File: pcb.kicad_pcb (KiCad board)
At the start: 2 copper layers, 88 x 53 mm, 40 parts, among them J1 TYPE-C-31-M-12, Q1 FDN339AN, SW1 SW_SPST, U1 WeMos_D1_mini, U2 TSOP38236, U3 MCP73831-2-OT, U4 BQ27441DRZR-G1A, U5 TLV75733PDBV

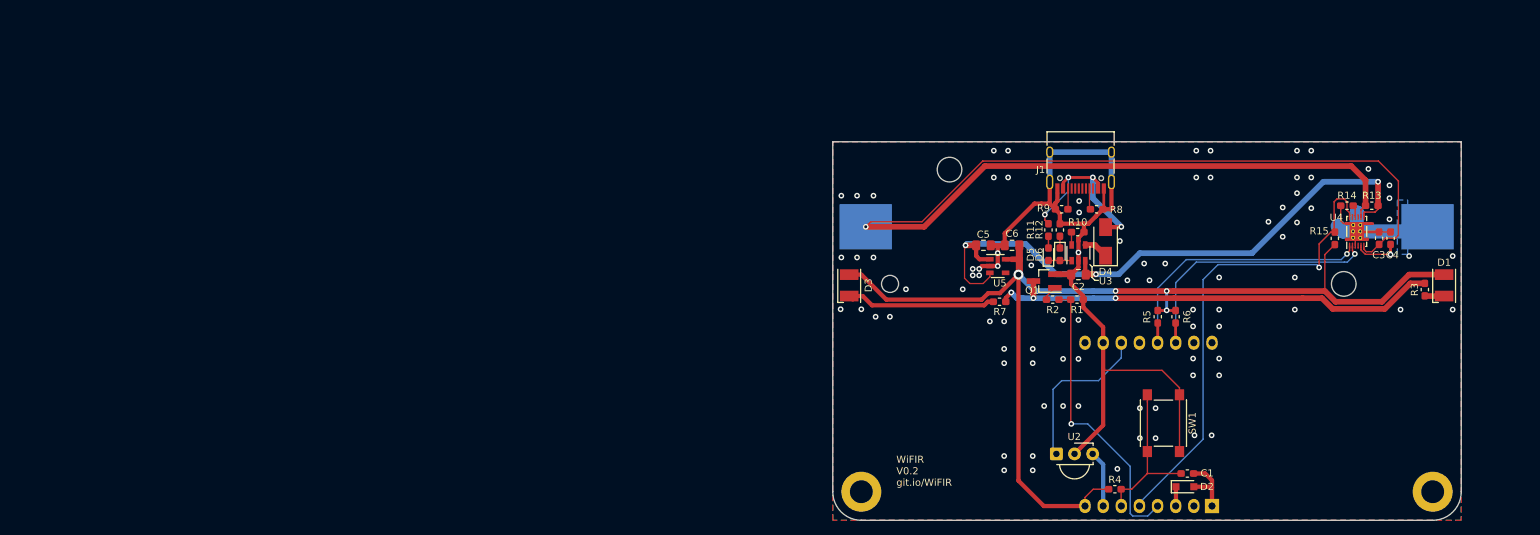
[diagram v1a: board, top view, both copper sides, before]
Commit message: Redesigned to small-stick formfactor
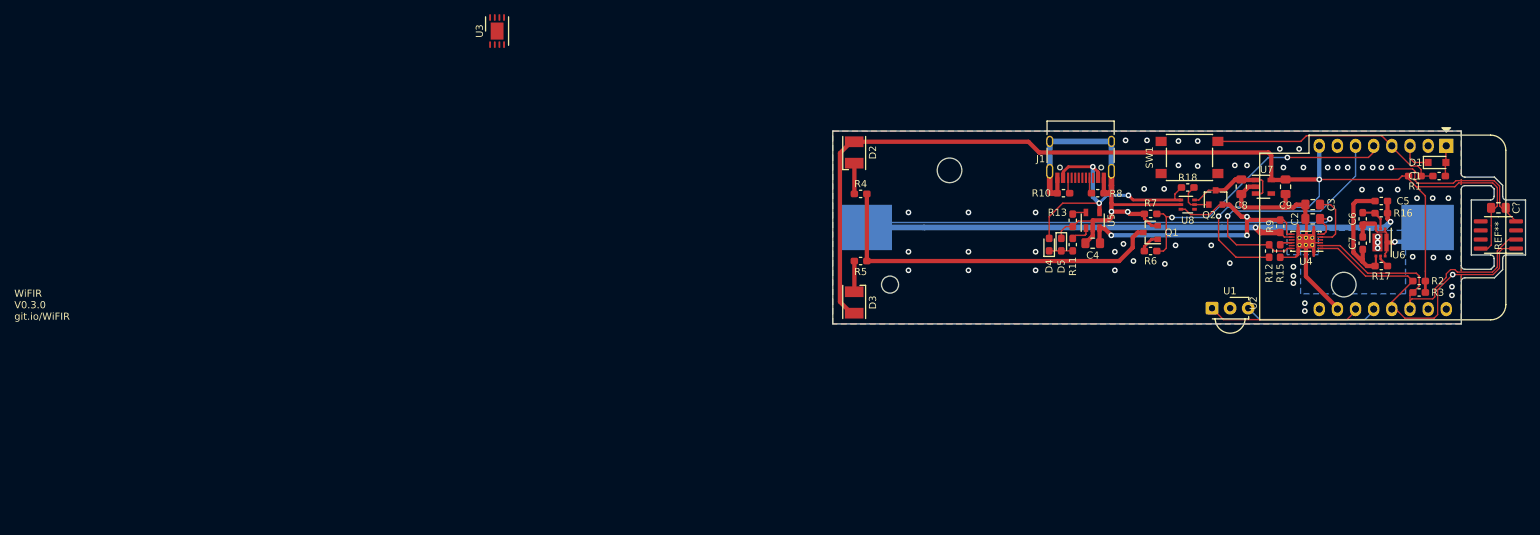
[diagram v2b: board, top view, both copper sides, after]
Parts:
- removed the C3 at (250.5, 77.5)
- removed D6: charged, LED_SMD:LED_0603_1608Metric_Pad1.05x0.95mm_HandSolder
- removed G*** (x2): LOGO, Personal_graphics:kiwi12.5mm
- removed the R15 at (244.3, 77.5)
- removed the REF** at (178.0, 113.0)
- removed the REF** at (258.0, 113.0)
- added C4: 4.7uF, Capacitor_SMD:C_0805_2012Metric_Pad1.15x1.40mm_HandSolder, F.Cu at (210.4, 78.2)
- added C7: 100nF, Capacitor_SMD:C_0603_1608Metric_Pad1.05x0.95mm_HandSolder, F.Cu at (248.2, 78.2)
- added C8: 4.7uF, Capacitor_SMD:C_0805_2012Metric_Pad1.15x1.40mm_HandSolder, F.Cu at (231.2, 70.3)
- added C9: 4.7uF, Capacitor_SMD:C_0805_2012Metric_Pad1.15x1.40mm_HandSolder, F.Cu at (237.4, 70.3)
- added C?: 10nF, Capacitor_SMD:C_0805_2012Metric_Pad1.15x1.40mm_HandSolder, F.Cu at (267.2, 73.2)
- added Q2: SI2333, Package_TO_SOT_SMD:SOT-23, F.Cu at (227.6, 71.8)
- added R16: 680R, Resistor_SMD:R_0603_1608Metric_Pad1.05x0.95mm_HandSolder, F.Cu at (250.8, 74.0)
- added R17: 1K, Resistor_SMD:R_0603_1608Metric_Pad1.05x0.95mm_HandSolder, F.Cu at (250.8, 81.4)
- added R18: 10k, Resistor_SMD:R_0603_1608Metric_Pad1.05x0.95mm_HandSolder, F.Cu at (223.7, 70.4)
- added REF**: SOIC-8_3.9x4.9mm_P1.27mm, Package_SO:SOIC-8_3.9x4.9mm_P1.27mm, F.Cu at (267.2, 77.0)
- added U6: LC05111C02MTTTG, Package_DFN_QFN:OnSemi_WDFN-6-2EP_2.6x4.0mm_P0.65mm, F.Cu at (250.7, 78.1)
- added U7: TLV75733PDBV, Package_TO_SOT_SMD:SOT-23-5, F.Cu at (234.3, 70.3)
- added U8: LM66100, Package_TO_SOT_SMD:SOT-363_SC-70-6, F.Cu at (223.7, 72.8)
- BT1: value protected 18650 -> Li-ion 3.7v
- C2: value 4.7uF -> 10nF
- C3: renamed from C4; footprint Capacitor_SMD:C_0603_1608Metric_Pad1.05x0.95mm_HandSolder -> Capacitor_SMD:C_0805_2012Metric_Pad1.15x1.40mm_HandSolder
- C5, C6: value 4.7uF -> 100nF; footprint Capacitor_SMD:C_0805_2012Metric_Pad1.15x1.40mm_HandSolder -> Capacitor_SMD:C_0603_1608Metric_Pad1.05x0.95mm_HandSolder
- D1: value VSML3710-GS18 -> BAT54WS; footprint LED_SMD:LED_PLCC-2 -> Diode_SMD:D_SOD-323_HandSoldering
- D2: value BAT54WS -> VSML3710-GS18; footprint Diode_SMD:D_SOD-323_HandSoldering -> LED_SMD:LED_PLCC-2
- D4: value MBRA140 -> charging; footprint Diode_SMD:D_SMA -> LED_SMD:LED_0603_1608Metric_Pad1.05x0.95mm_HandSolder
- D5: value charging -> charged
- Q1: footprint Package_TO_SOT_SMD:SOT-23_Handsoldering -> Package_TO_SOT_SMD:SOT-23
- R1: value 4k7 -> 10k
- R10: value 10k -> 5k1
- R12: value 470R -> 10k
- R13: value 10mR -> 2k2
- R2: value 1k -> 4k7
- R3, R7: value 6R8 -> 4k7
- R4: value 10k -> 6R8
- R5: value 4k7 -> 6R8
- R6: value 4k7 -> 1k
- R9: value 5k1 -> 10mR
- U1: value WeMos_D1_mini -> TSOP38236; footprint Module:WEMOS_D1_mini_light -> OptoDevice:Vishay_MINICAST-3Pin; moved to F.Cu
- U2: value TSOP38236 -> WeMos_D1_mini; footprint OptoDevice:Vishay_MINICAST-3Pin -> Module:WEMOS_D1_mini_light
- U3: value MCP73831-2-OT -> LC709203FQH-01TWG; footprint Package_TO_SOT_SMD:SOT-23-5 -> Package_DFN_QFN:WDFN-8-1EP_4x3mm_P0.65mm_EP2.4x1.8mm
- U5: value TLV75733PDBV -> MCP73831-2-OT
- moved U3 87.1 mm to (127.0, 48.5)
- moved U2 69.6 mm to (259.9, 64.6), turned to 270 degrees
- moved D2 65.8 mm to (177.0, 65.5), turned to 90 degrees
- moved C5 56.0 mm to (250.8, 72.3)
- moved C1 54.6 mm to (258.9, 68.8)
- moved R4 54.6 mm to (177.9, 71.3), turned to 0 degrees
- moved R2 51.4 mm to (256.1, 83.5), turned to 0 degrees
- moved R1 50.4 mm to (255.5, 68.8)
- moved C6 49.2 mm to (248.2, 74.8), turned to 90 degrees
- moved R5 42.3 mm to (177.9, 80.7), turned to 0 degrees
- moved R13 41.9 mm to (207.6, 75.0), turned to 90 degrees
- moved SW1 37.4 mm to (223.9, 66.2), turned to 180 degrees
- moved C2 33.7 mm to (241.2, 74.8)
- moved R9 30.7 mm to (236.7, 75.8), turned to 90 degrees
- moved R12 29.4 mm to (235.1, 79.3), turned to 270 degrees
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- renumbered R14 to R15
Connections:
- BT1 pad 2: GND -> -BATT
- C2 pad 2: VCCQ -> +BATT
- C5 pad 1: VCCQ -> GND
- C5 pad 2: GND -> +BATT
- C6 pad 1: GND -> -BATT
- C6 pad 2: +3V3 -> Net-(C6-Pad2)
- D1 pad 1: Net-(D1-Pad1) -> device_wake
- D1 pad 2: +3V3 -> ~RST
- D2 pad 1: device_wake -> Net-(D2-Pad1)
- D2 pad 2: ~RST -> +3V3
- D5 pad 1: Net-(D5-Pad1) -> GND
- D5 pad 2: Net-(D5-Pad2) -> Net-(D4-Pad1)
- R1 pad 1: GND -> factory_rst
- R1 pad 2: IR_BLAST -> +3V3
- R10 pad 2: Net-(R10-Pad2) -> Net-(J1-PadB5)
- R11 pad 1: VBUS -> Net-(D4-Pad1)
- R11 pad 2: Net-(D5-Pad2) -> Net-(R11-Pad2)
- R12 pad 1: Net-(D6-Pad1) -> ~LOW_BAT
- R12 pad 2: GND -> +3V3
- R13 pad 1: +BATT -> GND
- R13 pad 2: VCCQ -> Net-(R13-Pad2)
- R2 pad 1: IR_BLAST -> /MCU + I/O/SDA
- R2 pad 2: Net-(Q1-Pad1) -> +3V3
- R3 pad 1: Net-(D1-Pad1) -> /MCU + I/O/SCL
- R3 pad 2: Net-(Q1-Pad3) -> +3V3
- R4 pad 1: factory_rst -> Net-(D2-Pad1)
- R4 pad 2: +3V3 -> Net-(Q1-Pad3)
- R5 pad 1: SDA -> Net-(D3-Pad1)
- R5 pad 2: +3V3 -> Net-(Q1-Pad3)
- R6 pad 1: SCL -> IR_BLAST
- R6 pad 2: +3V3 -> Net-(Q1-Pad1)
- R7 pad 1: Net-(D3-Pad1) -> GND
- R7 pad 2: Net-(Q1-Pad3) -> IR_BLAST
- R9 pad 1: GND -> +BATT
- R9 pad 2: Net-(J1-PadB5) -> Net-(C4-Pad2)
- U1 pad 1: ~RST -> IR_SIGNAL
- U1 pad 2: Net-(U1-Pad2) -> GND
- U1 pad 3: device_wake -> IR_RECV_VCC
- U2 pad 1: IR_SIGNAL -> ~RST
- U2 pad 2: GND -> Net-(U2-Pad2)
- U2 pad 3: IR_RECV_VCC -> device_wake
- U3 pad 1: Net-(D5-Pad1) -> Net-(U3-Pad1)
- U3 pad 2: GND -> Net-(U3-Pad2)
- U3 pad 3: VCCQ -> Net-(U3-Pad3)
- U3 pad 4: Net-(D4-Pad1) -> Net-(U3-Pad4)
- U3 pad 5: Net-(R10-Pad2) -> Net-(U3-Pad5)
- U4 pad 1: SDA -> /MCU + I/O/SDA
- U4 pad 2: SCL -> /MCU + I/O/SCL
- U4 pad 7: VCCQ -> Net-(C4-Pad2)
- U5 pad 1: VCCQ -> Net-(R11-Pad2)
- U5 pad 3: VCCQ -> Net-(C4-Pad2)
- U5 pad 4: Net-(U5-Pad4) -> VBUS
- U5 pad 5: +3V3 -> Net-(R13-Pad2)
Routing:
- net VCCQ: track 89.6 -> 0.00 mm, vias 3 -> 0
- net /MCU + I/O/SDA: track 0.00 -> 45.5 mm, vias 0 -> 1
- net Net-(C4-Pad2): track 0.00 -> 44.8 mm, vias 0 -> 3
- net /MCU + I/O/SCL: track 0.00 -> 42.9 mm
- net SDA: track 40.3 -> 0.00 mm, vias 1 -> 0
- net SCL: track 39.4 -> 0.00 mm, vias 1 -> 0
- net ~LOW_BAT: track 67.6 -> 37.3 mm
- net +3V3: track 152.3 -> 181.7 mm, vias 4 -> 2
- net +BATT: track 173.7 -> 154.2 mm, vias 1 -> 3
- net Net-(D3-Pad1): track 21.6 -> 4.31 mm
- net -BATT: track 0.00 -> 17.1 mm, vias 0 -> 1
- net VBUS: track 26.2 -> 40.4 mm, vias 4 -> 3
- net Net-(Q1-Pad3): track 64.4 -> 50.6 mm, vias 3 -> 0
- net Net-(C8-Pad1): track 0.00 -> 13.5 mm
- net IR_RECV_VCC: track 7.91 -> 19.0 mm
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- added copper zone on B.Cu, net Net-(U6-Pad7)
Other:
- board size 88 x 53 mm -> 97 x 27 mm
- board text added: "WiFIR V0.3.0 git.io/WiFIR"
- board text removed: "JLCJLCJLCJLC"
- board text removed: "WiFIR V0.2 git.io/WiFIR"

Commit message: Added alternative fuel gauge to PCB
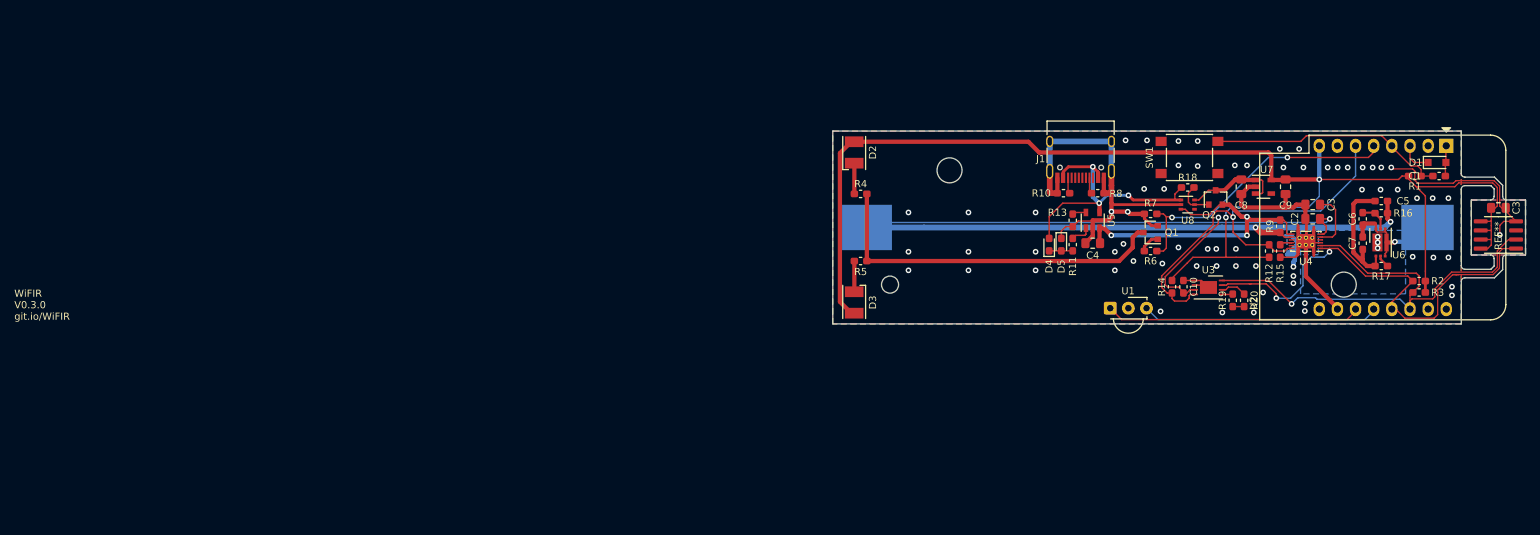
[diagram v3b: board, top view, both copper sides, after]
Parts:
- added C10: 1uF, Capacitor_SMD:C_0603_1608Metric_Pad1.05x0.95mm_HandSolder, F.Cu at (223.1, 84.3)
- added R14: 10k, Resistor_SMD:R_0603_1608Metric_Pad1.05x0.95mm_HandSolder, F.Cu at (221.5, 84.3)
- added R19: 10k, Resistor_SMD:R_0603_1608Metric_Pad1.05x0.95mm_HandSolder, F.Cu at (230.0, 86.2)
- added R20: 100R, Resistor_SMD:R_0603_1608Metric_Pad1.05x0.95mm_HandSolder, F.Cu at (231.6, 86.2)
- moved U3 105.9 mm to (226.6, 84.4), turned to 0 degrees
- moved U1 14.2 mm to (212.8, 87.3)
- gave numbers to parts that had none: 1
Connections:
- C3 pad 2: +3V3 -> +1V8
- REF** pad 5: (no net) -> +3V3
- REF** pad 6: (no net) -> +3V3
- REF** pad 7: (no net) -> +3V3
- U3 pad 1: Net-(U3-Pad1) -> GND
- U3 pad 2: Net-(U3-Pad2) -> GND
- U3 pad 3: Net-(U3-Pad3) -> +BATT
- U3 pad 4: Net-(U3-Pad4) -> ~LOW_BAT
- U3 pad 7: Net-(U3-Pad7) -> /MCU + I/O/SDA
- U3 pad 8: Net-(U3-Pad8) -> /MCU + I/O/SCL
- U3 pad 9: Net-(U3-Pad9) -> GND
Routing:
- net /MCU + I/O/SCL: track 42.9 -> 71.0 mm, vias 0 -> 1
- net /MCU + I/O/SDA: track 45.5 -> 67.8 mm, vias 1 -> 2
- net GND: track 149.6 -> 171.4 mm, vias 56 -> 66
- net ~LOW_BAT: track 37.3 -> 59.0 mm
- net +BATT: track 154.2 -> 172.4 mm, vias 3 -> 4
- net IR_SIGNAL: track 21.5 -> 35.8 mm
- net IR_RECV_VCC: track 19.0 -> 33.2 mm
- net +3V3: track 181.7 -> 195.0 mm
- net Net-(R20-Pad1): track 0.00 -> 3.66 mm
- net Net-(R19-Pad2): track 0.00 -> 1.63 mm
- net Net-(R19-Pad1): track 0.00 -> 1.60 mm

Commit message: Added stuff
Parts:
- removed the C3 at (267.2, 73.2)
- added C1: 1uF, Capacitor_SMD:C_0603_1608Metric_Pad1.05x0.95mm_HandSolder, F.Cu at (267.2, 73.2)
- U9: renamed from REF**; value SOIC-8_3.9x4.9mm_P1.27mm -> LM75C
- renumbered C1 to C11
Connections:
- U2 pad 6: ~LOW_BAT -> /MCU + I/O/Temp_O.S.
- U2 pad 7: Net-(U2-Pad7) -> ~LOW_BAT
- U9 pad 3: (no net) -> /MCU + I/O/Temp_O.S.
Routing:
- net /MCU + I/O/Temp_O.S.: track 0.00 -> 34.3 mm, vias 0 -> 1
- net /MCU + I/O/SCL: track 71.0 -> 78.4 mm
- net /MCU + I/O/SDA: track 67.8 -> 60.6 mm, vias 2 -> 4
- net GND: track 171.4 -> 168.9 mm, vias 66 -> 63
- net ~LOW_BAT: track 59.0 -> 57.9 mm
